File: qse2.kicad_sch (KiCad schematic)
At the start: 71 parts, among them J1 5-1814832-1, J2 5-1814832-1, J3 Conn_02x08_Odd_Even, J4 SJ-3524-SMT, J6 Conn_01x02, U1 SN74LVC1G14DBV, U2 SN74LVC1G14DBV, U3 SN74CBT3253, U4 SN74AC74PW, U5 AD8137ARZ-R7, U6 NCP115ASN330T2G, U7 UA78M05IDCYR, U8 AP2120N-2.5TRG1, U9 AD8137ARZ-R7

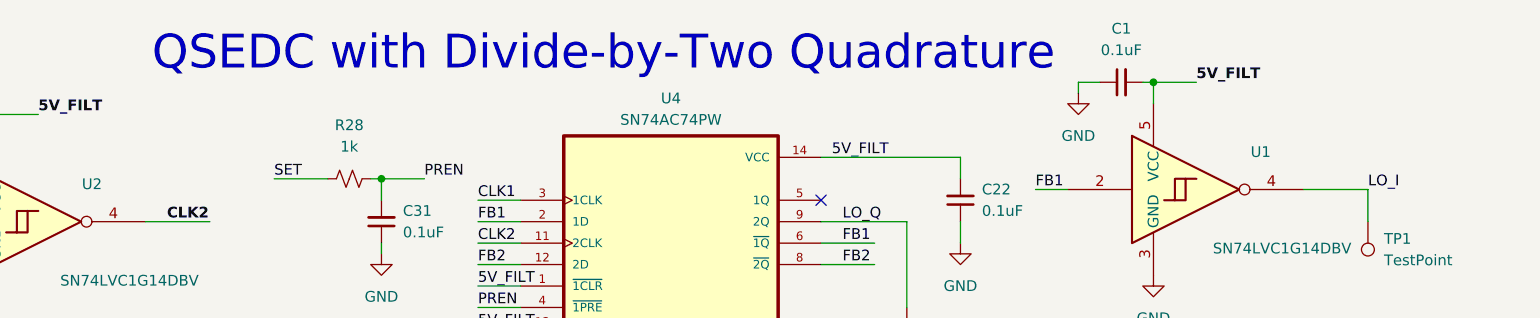
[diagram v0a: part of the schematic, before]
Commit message: Minor change to schematic text.
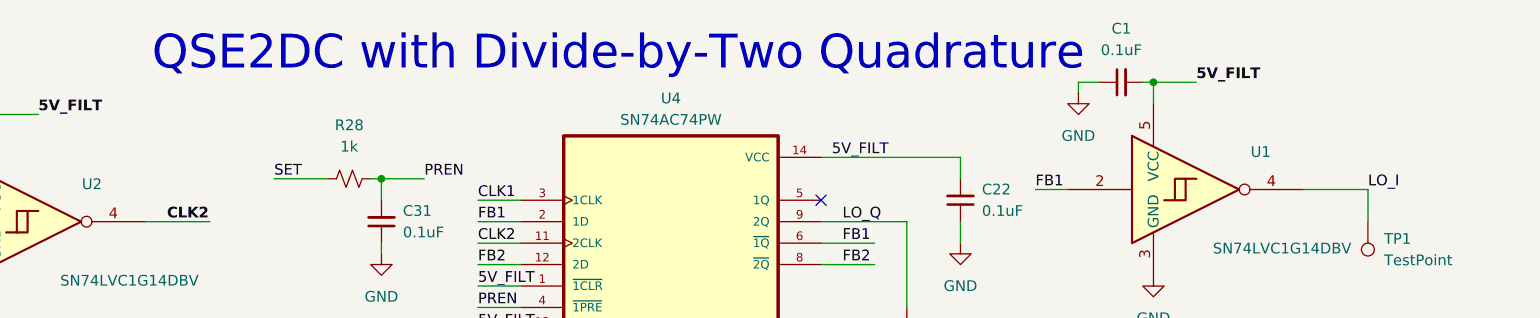
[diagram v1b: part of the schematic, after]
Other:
- note added: "QSE2DC with Divide-by-Two Quadrature"
- note removed: "QSEDC with Divide-by-Two Quadrature"

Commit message: Final gerbers before June release to PCB.
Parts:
- added C11, C13: 1uF, Capacitor_SMD:C_1206_3216Metric, symbol Device:C_Small
- added C12, C7, C9: 0.1uF, Capacitor_SMD:C_1206_3216Metric, symbol Device:C_Small
- added J7: B4B-XH-A_LF__SN_, digikey-footprints:PinHeader_1x4_P2.5mm_Drill1.1mm, symbol dk_Rectangular-Connectors-Headers-Male-Pins:B4B-XH-A_LF__SN_
- added U10: SN74LVC1G14DBV, Package_TO_SOT_SMD:SOT-23-5, symbol 74xGxx:SN74LVC1G14DBV
- added U11: NCP508SQ33T1G, TSOP-5-483-N_ONS, symbol NCP508SQ33T1G:NCP508SQ33T1G
- R5, R7: value 1000 -> 4.7k
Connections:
- net 5V_FILT: now also U6.3 (EN), C12.2, C13.1, C9.2, J7.1, U11.1 (VIN), U11.3 (ENABLE); no longer C1.2, C10.2, C22.2, C6.2, R7.2, U1.5 (VCC), U2.5 (VCC), U4.1 (~{1CLR}), U4.13 (~{2CLR}), U4.14 (VCC)
- net CLK1: now also U10.4; no longer J1.2
- net GND: now also C11.2, C12.1, C13.2, C7.1, C9.1, J7.2, U10.3 (GND), U11.2 (GND); no longer R5.1
- net SDA: now reaches J3.3 (Pin_3)
- net SDA: now also R5.2, J7.4
- net SCL: now reaches J3.4 (Pin_4)
- net SCL: now also R7.2, J7.3
- new net: J1.2, U10.2
- new net 3_3V: C1.2, C10.2, C11.1, C22.2, C6.2, C7.2, R5.1, R7.1, U1.5 (VCC), U10.5 (VCC), U11.4 (NC), U11.5 (VOUT), U2.5 (VCC), U4.1 (~{1CLR}), U4.13 (~{2CLR}), U4.14 (VCC)
- no-connect marks 8 -> 6
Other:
- note added: "3.3 VOLT REGULATOR"
- moved on the sheet: C1, C10, C22, C31, C6, J1, J6, R28, R9, TP1, TP2, U1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

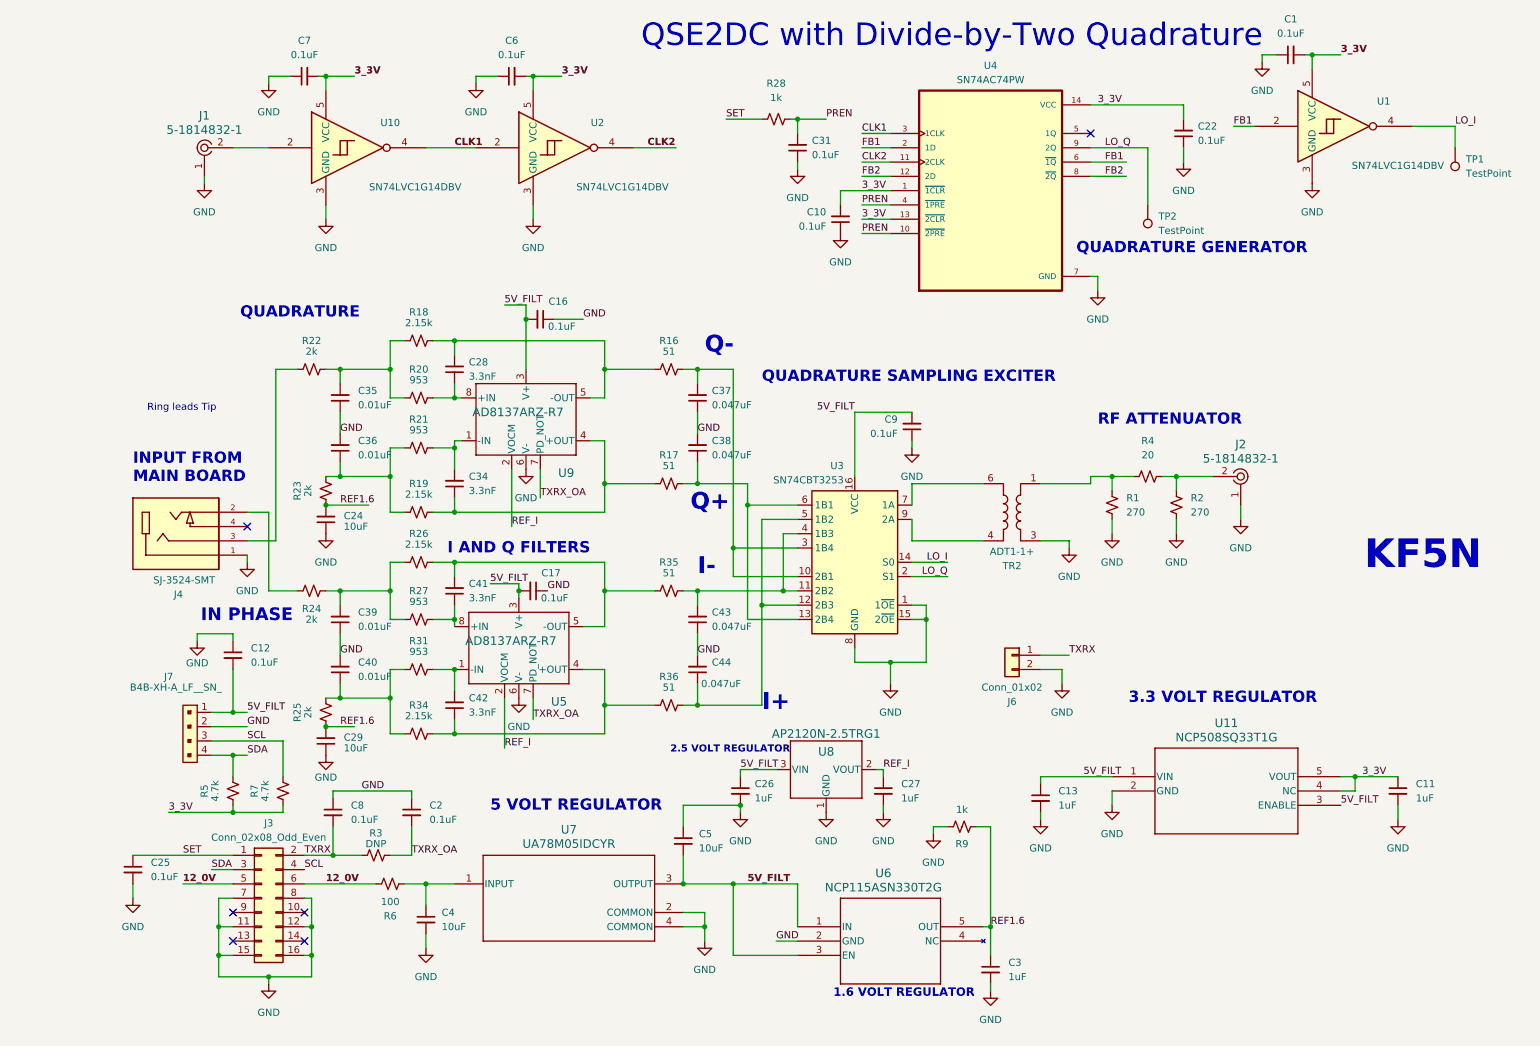
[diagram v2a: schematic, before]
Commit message: Mostly cleaned up version with SOICs replacing TSOPs.
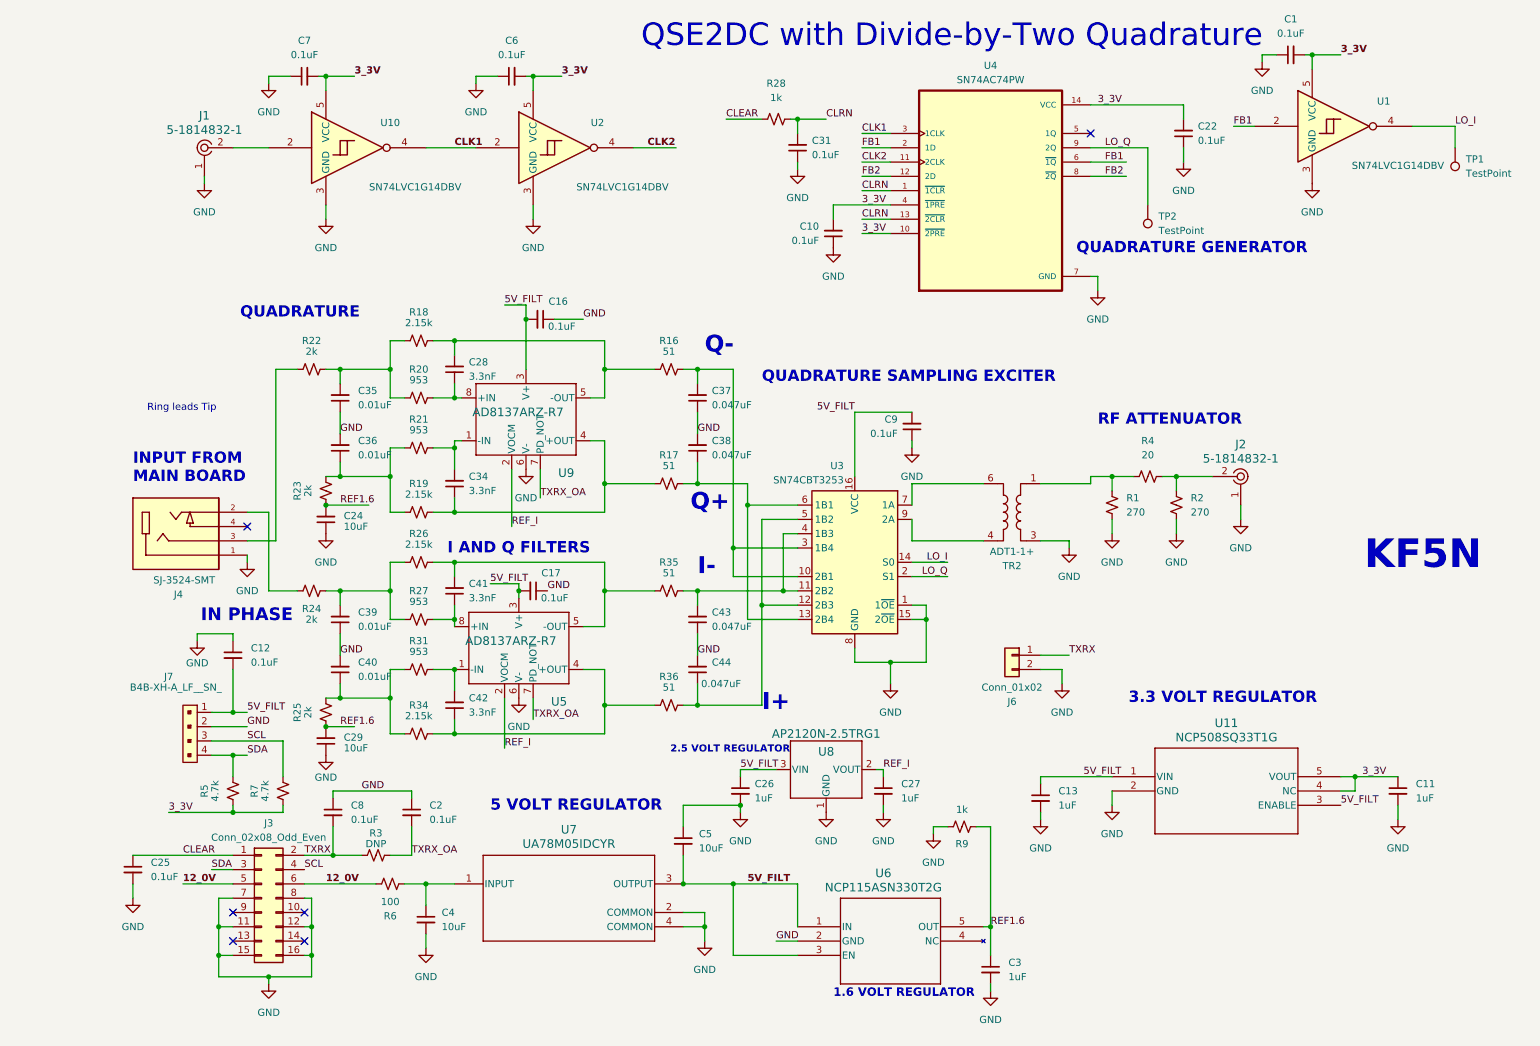
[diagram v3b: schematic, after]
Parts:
- U3: footprint Package_SO:TSSOP-16_4.4x5mm_P0.65mm -> Package_SO:SOIC-16_3.9x9.9mm_P1.27mm
- U4: footprint Package_SO:TSSOP-14_4.4x5mm_P0.65mm -> Package_SO:SOIC-14_3.9x8.7mm_P1.27mm
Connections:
- net 3_3V: now also U4.10 (~{2PRE}), U4.4 (~{1PRE}); no longer U4.1 (~{1CLR}), U4.13 (~{2CLR})
- net PREN renamed CLRN
- net CLRN: now also U4.1 (~{1CLR}), U4.13 (~{2CLR}); no longer U4.10 (~{2PRE}), U4.4 (~{1PRE})
- net SET renamed CLEAR
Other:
- moved on the sheet: C10
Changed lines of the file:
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@@
 	(wire
 		(pts
-			(xy 142.24 46.99) (xy 142.24 49.53)
+			(xy 146.05 46.99) (xy 151.13 46.99)
 		)
 		(stroke
@@
 	(wire
 		(pts
-			(xy 146.05 52.07) (xy 151.13 52.07)
-		)
-		(stroke
-			(width 0)
-			(type default)
-		)
-	)
-	(wire
-		(pts
 			(xy 219.71 22.86) (xy 217.17 22.86)
 		)
@@
 	(wire
 		(pts
+			(xy 140.97 52.07) (xy 140.97 49.53)
+		)
+		(stroke
+			(width 0)
+			(type default)
+		)
+	)
+	(wire
+		(pts
 			(xy 53.34 95.25) (xy 53.34 97.79)
 		)
@@
 	(wire
 		(pts
-			(xy 142.24 46.99) (xy 151.13 46.99)
-		)
-		(stroke
-			(width 0)
-			(type default)
-		)
-	)
-	(wire
-		(pts
 			(xy 154.94 109.22) (xy 167.64 109.22)
 		)
@@
 	(wire
 		(pts
+			(xy 140.97 49.53) (xy 151.13 49.53)
+		)
+		(stroke
+			(width 0)
+			(type default)
+		)
+	)
+	(wire
+		(pts
 			(xy 44.45 26.67) (xy 40.64 26.67)
 		)
@@
 	(wire
 		(pts
+			(xy 146.05 52.07) (xy 151.13 52.07)
+		)
+		(stroke
+			(width 0)
+			(type default)
+		)
+	)
+	(wire
+		(pts
 			(xy 186.69 39.37) (xy 196.85 39.37)
 		)
@@
 	(wire
 		(pts
-			(xy 146.05 49.53) (xy 151.13 49.53)
-		)
-		(stroke
-			(width 0)
-			(type default)
-		)
-	)
-	(wire
-		(pts
 			(xy 186.69 44.45) (xy 193.04 44.45)
 		)
@@
 		)
 	)
-	(label "PREN"
+	(label "3_3V"
 		(at 146.05 54.61 0)
 		(fields_autoplaced yes)
@@
 		)
 	)
-	(label "PREN"
+	(label "CLRN"
 		(at 139.7 34.29 0)
 		(fields_autoplaced yes)
@@
 		)
 	)
-	(label "3_3V"
+	(label "CLRN"
 		(at 146.05 52.07 0)
 		(fields_autoplaced yes)
@@
 		)
 	)
-	(label "3_3V"
+	(label "CLRN"
 		(at 146.05 46.99 0)
 		(fields_autoplaced yes)
@@
 		)
 	)
-	(label "SET"
+	(label "CLEAR"
 		(at 25.4 165.1 0)
 		(fields_autoplaced yes)
@@
 		)
 	)
-	(label "PREN"
+	(label "3_3V"
 		(at 146.05 49.53 0)
 		(fields_autoplaced yes)
@@
 		)
 	)
-	(label "SET"
+	(label "CLEAR"
 		(at 121.92 34.29 0)
 		(fields_autoplaced yes)
@@
 			)
 		)
-		(property "Footprint" "Package_SO:TSSOP-14_4.4x5mm_P0.65mm"
+		(property "Footprint" "Package_SO:SOIC-14_3.9x8.7mm_P1.27mm"
 			(at 168.91 46.99 0)
 			(effects
@@
 	(symbol
 		(lib_id "Device:C_Small")
-		(at 142.24 52.07 0)
+		(at 140.97 54.61 0)
 		(mirror x)
 		(unit 1)
@@
 		(fields_autoplaced yes)
 		(property "Reference" "C10"
-			(at 139.7 50.7936 0)
+			(at 138.43 53.3336 0)
 			(effects
 				(font
@@
 		)
 		(property "Value" "0.1uF"
-			(at 139.7 53.3336 0)
+			(at 138.43 55.8736 0)
 			(effects
 				(font
@@
 		)
 		(property "Footprint" "Capacitor_SMD:C_1206_3216Metric"
-			(at 142.24 52.07 0)
+			(at 140.97 54.61 0)
 			(effects
 				(font
@@
 		)
 		(property "Datasheet" "~"
-			(at 142.24 52.07 0)
+			(at 140.97 54.61 0)
 			(effects
 				(font
@@
 		)
 		(property "Description" "Unpolarized capacitor, small symbol"
-			(at 142.24 52.07 0)
+			(at 140.97 54.61 0)
 			(effects
 				(font
@@
 	(symbol
 		(lib_id "power:GND")
-		(at 142.24 54.61 0)
+		(at 140.97 57.15 0)
 		(mirror y)
 		(unit 1)
@@
 		(fields_autoplaced yes)
 		(property "Reference" "#PWR016"
-			(at 142.24 60.96 0)
+			(at 140.97 63.5 0)
 			(effects
 				(font
@@
 		)
 		(property "Value" "GND"
-			(at 142.24 59.69 0)
+			(at 140.97 62.23 0)
 			(effects
 				(font
@@
 		)
 		(property "Footprint" ""
-			(at 142.24 54.61 0)
+			(at 140.97 57.15 0)
 			(effects
 				(font
@@
 		)
 		(property "Datasheet" ""
-			(at 142.24 54.61 0)
+			(at 140.97 57.15 0)
 			(effects
 				(font
@@
 		)
 		(property "Description" "Power symbol creates a global label with name \"GND\" , ground"
-			(at 142.24 54.61 0)
+			(at 140.97 57.15 0)
 			(effects
 				(font
@@
 			)
 		)
-		(property "Footprint" "Package_SO:TSSOP-16_4.4x5mm_P0.65mm"
+		(property "Footprint" "Package_SO:SOIC-16_3.9x9.9mm_P1.27mm"
 			(at 144.78 113.03 0)
 			(effects

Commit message: Ready to release V1.1 June 30.
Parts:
- added C14, C15: 10uF, Capacitor_SMD:C_1206_3216Metric, symbol Device:C_Small
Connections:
- net GND: now also C14.1, C15.1
- net REF1.6: now also C14.2, C15.2
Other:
- moved on the sheet: C24, C29

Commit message: Updated README and very minor update to Gerbers.
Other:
- note added: "QSE2DCEZ with Divide-by-Two Quadrature"
- note removed: "QSE2DC with Divide-by-Two Quadrature"
- title: QSE2DC with Divide-by-Two Quadrature -> QSE2DCEZ with Divide-by-Two Quadrature
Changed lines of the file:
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@@
 	(paper "A4")
 	(title_block
-		(title "QSE2DC with Divide-by-Two Quadrature")
-		(date "2024-06-18")
+		(title "QSE2DCEZ with Divide-by-Two Quadrature")
+		(date "2024-07-26")
 		(rev "1.1")
 	)
@@
 		)
 	)
-	(text "QSE2DC with Divide-by-Two Quadrature"
+	(text "QSE2DCEZ with Divide-by-Two Quadrature"
 		(exclude_from_sim no)
 		(at 106.807 21.844 0)

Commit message: Added notes to schematic.
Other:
- note added: "DON'T PLACE J7 R5 R7"
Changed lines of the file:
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@@
+		)
+	)
+	(text "DON'T PLACE\nJ7 R5 R7"
+		(exclude_from_sim no)
+		(at 18.415 144.145 0)
+		(effects
+			(font
+				(size 1.27 1.27)
+			)
 		)
 	)

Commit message: Fixed regulator part numbers on schematic.
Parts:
- U11: value NCP508SQ33T1G -> NCP114ASN330T1G
- U6: value NCP115ASN330T2G -> NCV8114ASN165T1G
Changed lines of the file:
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@@
 		(fields_autoplaced yes)
 		(property "Reference" "U11"
-			(at 210.82 141.605 0)
+			(at 210.82 140.97 0)
 			(effects
 				(font
@@
 			)
 		)
-		(property "Value" "NCP508SQ33T1G"
-			(at 210.82 144.145 0)
+		(property "Value" "NCP114ASN330T1G"
+			(at 210.82 143.51 0)
 			(effects
 				(font
@@
 			)
 		)
-		(property "Value" "NCP115ASN330T2G"
+		(property "Value" "NCV8114ASN165T1G"
 			(at 149.86 170.815 0)
 			(effects

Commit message: Release to fab.
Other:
- note added: "SWITCH SDA AND SCL"
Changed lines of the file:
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@@
+		)
+	)
+	(text "SWITCH SDA AND SCL"
+		(exclude_from_sim no)
+		(at 34.29 143.51 0)
+		(effects
+			(font
+				(size 4 4)
+				(thickness 0.8)
+				(bold yes)
+			)
 		)
 	)
